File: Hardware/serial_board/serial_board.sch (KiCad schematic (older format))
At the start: 11 parts, among them J1 Conn_01x40, J2 Conn_01x06, U1 W65C51NxP, X1 CXO_DIP8

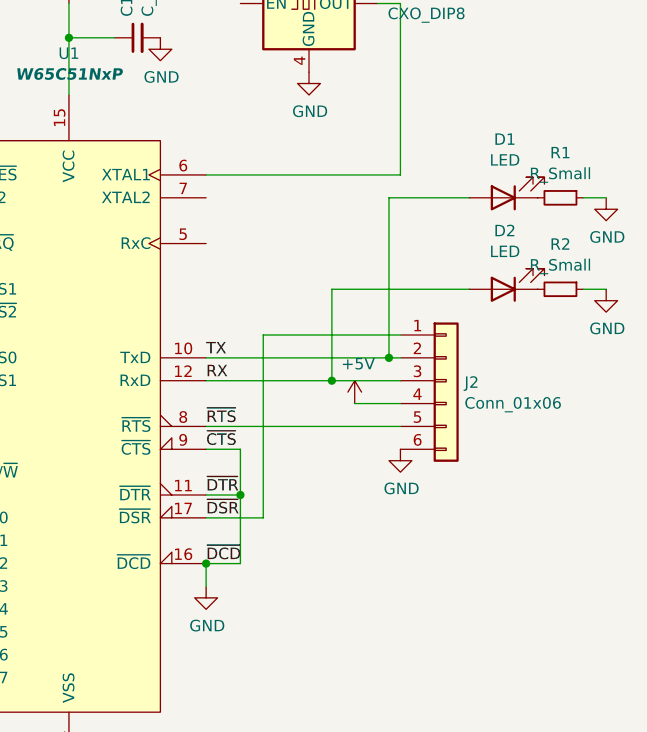
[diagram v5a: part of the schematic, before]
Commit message: Update serial board with through hole components
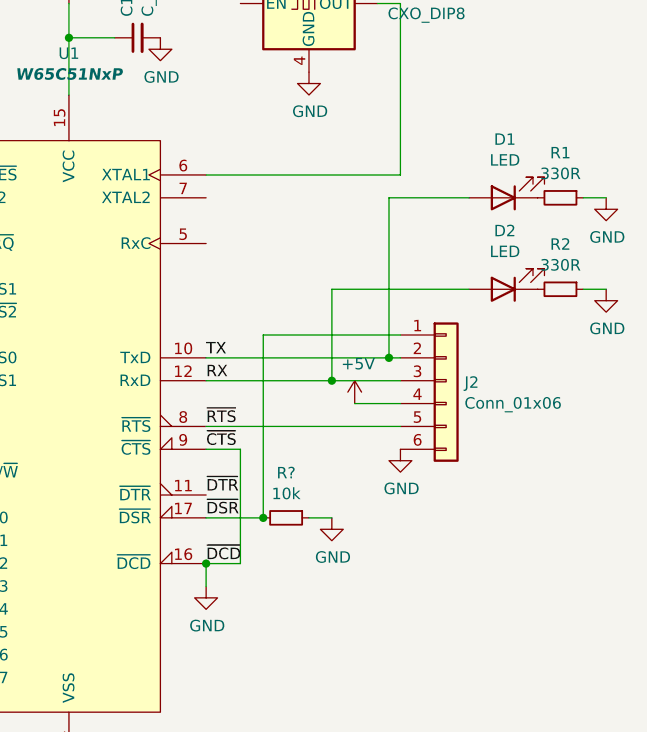
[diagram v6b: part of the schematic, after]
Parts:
- added R?: 10k, Resistor_THT:R_Axial_DIN0204_L3.6mm_D1.6mm_P5.08mm_Horizontal, symbol Device:R_Small
- C1, C2: footprint Capacitor_SMD:C_1206_3216Metric_Pad1.42x1.75mm_HandSolder -> Capacitor_THT:C_Disc_D4.3mm_W1.9mm_P5.00mm
- D1, D2: footprint LED_SMD:LED_1206_3216Metric_Pad1.42x1.75mm_HandSolder -> LED_THT:LED_D3.0mm
- R1, R2: value R_Small -> 330R; footprint Resistor_SMD:R_0805_2012Metric_Pad1.15x1.40mm_HandSolder -> Resistor_THT:R_Axial_DIN0204_L3.6mm_D1.6mm_P5.08mm_Horizontal
- R3: footprint Resistor_SMD:R_0805_2012Metric_Pad1.15x1.40mm_HandSolder -> Resistor_THT:R_Axial_DIN0204_L3.6mm_D1.6mm_P5.08mm_Horizontal
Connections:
- net GND: now also R?.1; no longer U1.11 (~DTR)
- net ~DSR~: now also R?.2
- new net ~DTR~: U1.11 (~DTR)
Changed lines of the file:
@@
 F 0 "C1" H 5692 1946 50  0000 L CNN
 F 1 "C_Small" H 5692 1855 50  0000 L CNN
-F 2 "Capacitor_SMD:C_1206_3216Metric_Pad1.42x1.75mm_HandSolder" H 5600 1900 50  0001 C CNN
+F 2 "Capacitor_THT:C_Disc_D4.3mm_W1.9mm_P5.00mm" H 5600 1900 50  0001 C CNN
 F 3 "~" H 5600 1900 50  0001 C CNN
 	1    5600 1900
@@
 F 0 "C2" H 6742 1246 50  0000 L CNN
 F 1 "C_Small" H 6742 1155 50  0000 L CNN
-F 2 "Capacitor_SMD:C_1206_3216Metric_Pad1.42x1.75mm_HandSolder" H 6650 1200 50  0001 C CNN
+F 2 "Capacitor_THT:C_Disc_D4.3mm_W1.9mm_P5.00mm" H 6650 1200 50  0001 C CNN
 F 3 "~" H 6650 1200 50  0001 C CNN
 	1    6650 1200
@@
 F 0 "D1" H 7193 2345 50  0000 C CNN
 F 1 "LED" H 7193 2436 50  0000 C CNN
-F 2 "LED_SMD:LED_1206_3216Metric_Pad1.42x1.75mm_HandSolder" H 7200 2600 50  0001 C CNN
+F 2 "LED_THT:LED_D3.0mm" H 7200 2600 50  0001 C CNN
 F 3 "~" H 7200 2600 50  0001 C CNN
 	1    7200 2600
@@
 P 7450 2600
 F 0 "R1" V 7254 2600 50  0000 C CNN
-F 1 "R_Small" V 7345 2600 50  0000 C CNN
-F 2 "Resistor_SMD:R_0805_2012Metric_Pad1.15x1.40mm_HandSolder" H 7450 2600 50  0001 C CNN
+F 1 "330R" V 7345 2600 50  0000 C CNN
+F 2 "Resistor_THT:R_Axial_DIN0204_L3.6mm_D1.6mm_P5.08mm_Horizontal" H 7450 2600 50  0001 C CNN
 F 3 "~" H 7450 2600 50  0001 C CNN
 	1    7450 2600
@@
 F 0 "D2" H 7193 2745 50  0000 C CNN
 F 1 "LED" H 7193 2836 50  0000 C CNN
-F 2 "LED_SMD:LED_1206_3216Metric_Pad1.42x1.75mm_HandSolder" H 7200 3000 50  0001 C CNN
+F 2 "LED_THT:LED_D3.0mm" H 7200 3000 50  0001 C CNN
 F 3 "~" H 7200 3000 50  0001 C CNN
 	1    7200 3000
@@
 P 7450 3000
 F 0 "R2" V 7254 3000 50  0000 C CNN
-F 1 "R_Small" V 7345 3000 50  0000 C CNN
-F 2 "Resistor_SMD:R_0805_2012Metric_Pad1.15x1.40mm_HandSolder" H 7450 3000 50  0001 C CNN
+F 1 "330R" V 7345 3000 50  0000 C CNN
+F 2 "Resistor_THT:R_Axial_DIN0204_L3.6mm_D1.6mm_P5.08mm_Horizontal" H 7450 3000 50  0001 C CNN
 F 3 "~" H 7450 3000 50  0001 C CNN
 	1    7450 3000
@@
 F 0 "R3" V 3804 3000 50  0000 C CNN
 F 1 "10k" V 3895 3000 50  0000 C CNN
-F 2 "Resistor_SMD:R_0805_2012Metric_Pad1.15x1.40mm_HandSolder" H 4000 3000 50  0001 C CNN
+F 2 "Resistor_THT:R_Axial_DIN0204_L3.6mm_D1.6mm_P5.08mm_Horizontal" H 4000 3000 50  0001 C CNN
 F 3 "~" H 4000 3000 50  0001 C CNN
 	1    4000 3000
@@
 	5900 4000 6150 4000
 Wire Wire Line
-	5900 3900 6050 3900
-Wire Wire Line
-	6050 3900 6050 3700
-Wire Wire Line
-	6050 3900 6050 4200
-Wire Wire Line
 	6050 4200 5900 4200
-Connection ~ 6050 3900
 Connection ~ 5900 4200
+$Comp
+L Device:R_Small R?
+U 1 1 612DC0C9
+P 6250 4000
+F 0 "R?" V 6054 4000 50  0000 C CNN
+F 1 "10k" V 6145 4000 50  0000 C CNN
+F 2 "Resistor_THT:R_Axial_DIN0204_L3.6mm_D1.6mm_P5.08mm_Horizontal" H 6250 4000 50  0001 C CNN
+F 3 "~" H 6250 4000 50  0001 C CNN
+	1    6250 4000
+	0    1    1    0
+$EndComp
+Wire Wire Line
+	6050 3700 6050 4200
+Connection ~ 6150 4000
+$Comp
+L power:GND #PWR?
+U 1 1 612DE816
+P 6450 4000
+F 0 "#PWR?" H 6450 3750 50  0001 C CNN
+F 1 "GND" H 6455 3827 50  0000 C CNN
+F 2 "" H 6450 4000 50  0001 C CNN
+F 3 "" H 6450 4000 50  0001 C CNN
+	1    6450 4000
+	1    0    0    -1
+$EndComp
+Wire Wire Line
+	6450 4000 6350 4000
 $EndSCHEMATC

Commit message: update gerbers for serial board
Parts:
- gave numbers to parts that had none: 1
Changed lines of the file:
@@
 Connection ~ 5900 4200
 $Comp
-L Device:R_Small R?
+L Device:R_Small R4
 U 1 1 612DC0C9
 P 6250 4000
-F 0 "R?" V 6054 4000 50  0000 C CNN
+F 0 "R4" V 6054 4000 50  0000 C CNN
 F 1 "10k" V 6145 4000 50  0000 C CNN
 F 2 "Resistor_THT:R_Axial_DIN0204_L3.6mm_D1.6mm_P5.08mm_Horizontal" H 6250 4000 50  0001 C CNN
@@
 Connection ~ 6150 4000
 $Comp
-L power:GND #PWR?
+L power:GND #PWR0117
 U 1 1 612DE816
 P 6450 4000
-F 0 "#PWR?" H 6450 3750 50  0001 C CNN
+F 0 "#PWR0117" H 6450 3750 50  0001 C CNN
 F 1 "GND" H 6455 3827 50  0000 C CNN
 F 2 "" H 6450 4000 50  0001 C CNN

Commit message: vertical leds
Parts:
- D1, D2: footprint LED_THT:LED_D3.0mm -> LED_THT:LED_D3.0mm_Horizontal_O3.81mm_Z2.0mm
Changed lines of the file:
@@
 F 0 "D1" H 7193 2345 50  0000 C CNN
 F 1 "LED" H 7193 2436 50  0000 C CNN
-F 2 "LED_THT:LED_D3.0mm" H 7200 2600 50  0001 C CNN
+F 2 "LED_THT:LED_D3.0mm_Horizontal_O3.81mm_Z2.0mm" H 7200 2600 50  0001 C CNN
 F 3 "~" H 7200 2600 50  0001 C CNN
 	1    7200 2600
@@
 F 0 "D2" H 7193 2745 50  0000 C CNN
 F 1 "LED" H 7193 2836 50  0000 C CNN
-F 2 "LED_THT:LED_D3.0mm" H 7200 3000 50  0001 C CNN
+F 2 "LED_THT:LED_D3.0mm_Horizontal_O3.81mm_Z2.0mm" H 7200 3000 50  0001 C CNN
 F 3 "~" H 7200 3000 50  0001 C CNN
 	1    7200 3000
